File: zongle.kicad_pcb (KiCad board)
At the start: 6 copper layers, 13.5 x 14.4 mm, 19 parts, among them U1 453-00059R

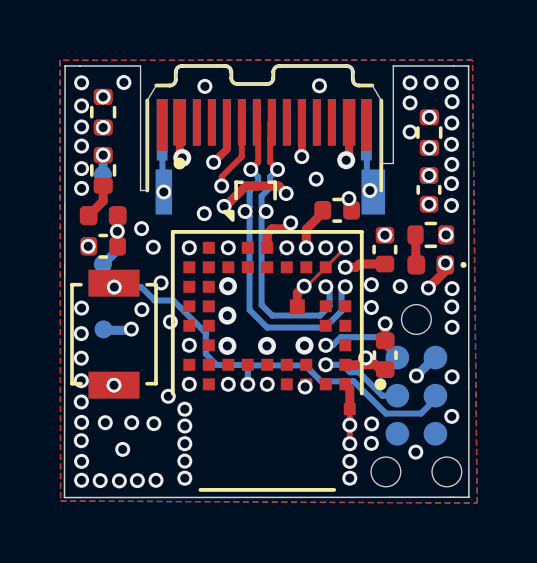
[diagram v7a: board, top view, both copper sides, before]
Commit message: some routing refinements. moved all components as far away from the antenna as possible. added another decup cap to the power path. changed board thickness to 0.8mm to accomodate for usb-c plug. some layout optimizations
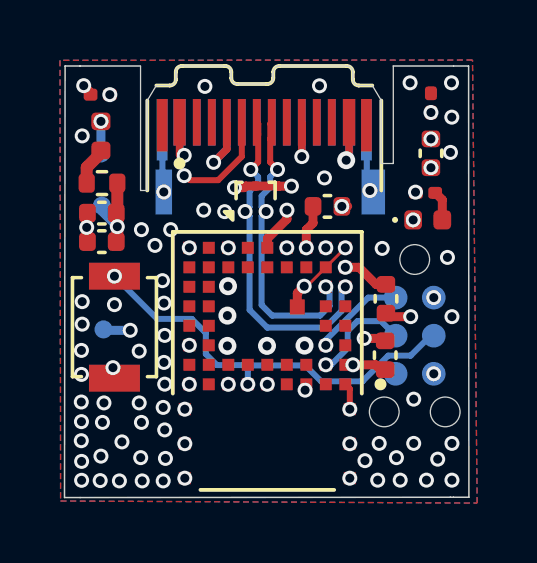
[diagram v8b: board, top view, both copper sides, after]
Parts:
- added C27: 10uF, Capacitor_SMD:C_0402_1005Metric, F.Cu at (146.3, 107.4)
- F1: value 750mA -> 500mA
- FB1: value 100 Ω @ 100 MHz -> BLM15PX121SN1D
- R21, R23, R26: footprint Resistor_SMD:R_0402_1005Metric -> Resistor_SMD:R_0201_0603Metric
- moved F1 2.66 mm to (146.2, 104.8), turned to -90 degrees
- moved SWD1 2.00 mm to (156.7, 111.5)
- moved Tp+5v1 1.96 mm to (146.3, 107.2)
- moved C11 1.64 mm to (155.7, 110.3), turned to 90 degrees
- moved LED_STATUS1 1.50 mm to (157.1, 107.7), turned to 0 degrees
- moved R21 1.41 mm to (157.0, 106.8), turned to 0 degrees
- moved C26 1.22 mm to (157.2, 105.4)
- moved R26 0.99 mm to (157.2, 103.8)
- moved TpVBUS1 0.72 mm to (146.2, 105.4)
- moved R23 0.59 mm to (146.2, 103.5), turned to 0 degrees
- moved FB1 0.43 mm to (146.3, 106.4), turned to 0 degrees
- moved C23 0.35 mm to (153.8, 107.2)
- moved SWReset_1 0.24 mm to (146.7, 111.2)
- moved C22 0.16 mm to (146.3, 108.4)
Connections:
- F1 pad 1: Net-(F1-Pad1) -> VBUS_Raw
- F1 pad 2: +5V -> Net-(F1-Pad2)
- FB1 pad 1: VBUS_Raw -> Net-(F1-Pad2)
- FB1 pad 2: Net-(F1-Pad1) -> +5V
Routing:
- net VBUS_Raw: track 16.2 -> 17.9 mm
- net +5V: track 14.3 -> 15.8 mm
- net VDD_NRF: track 10.0 -> 11.3 mm
- net Net-(F1-Pad1): track 1.20 -> 0.00 mm
- net Net-(F1-Pad2): track 0.00 -> 1.20 mm
- net LED_ST: track 4.94 -> 3.98 mm
- net GND: track 16.7 -> 15.8 mm, vias 95 -> 92
- net Net-(C26-Pad1): track 18.1 -> 18.9 mm
- net SWCLK: track 2.81 -> 3.47 mm
